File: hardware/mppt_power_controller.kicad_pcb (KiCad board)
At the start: 2 copper layers, 100 x 50 mm, 55 parts, among them J1 Solar Input, J2 USB_B_Micro, J3 Conn_ARM_JTAG_SWD_10, J4 Battery, J5 Curiosity Board, Q1 Q_NMOS_GSD, Q2 Q_NMOS_GSD, U1 INA233, U2 PX3519, U3 ATSAMD21G18A-AUT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

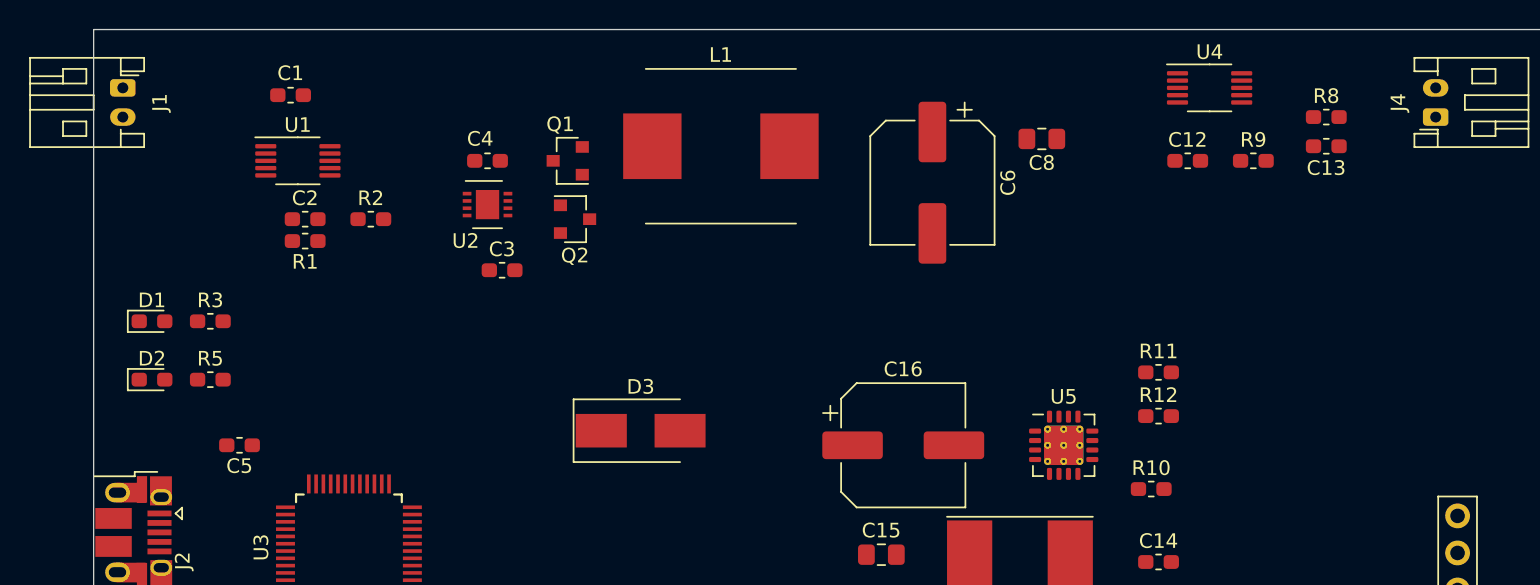
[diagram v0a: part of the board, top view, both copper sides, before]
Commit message: Routed a good portion of the buck converter and the first voltage/current monitor.
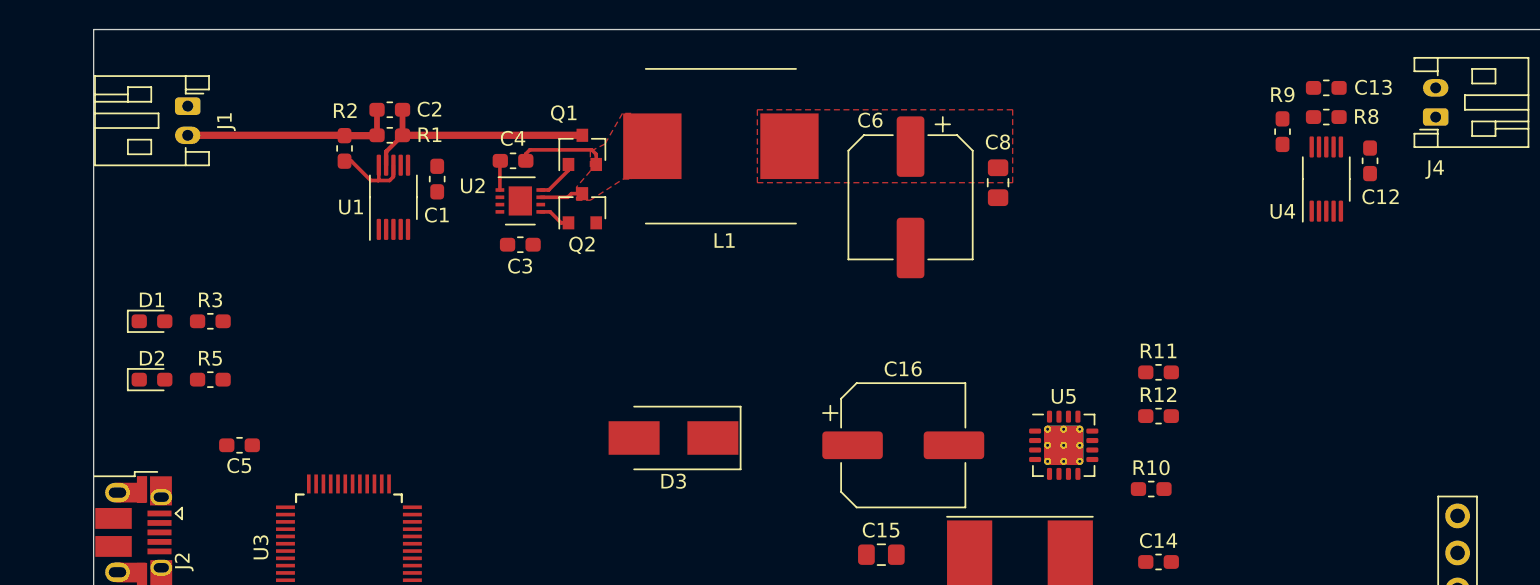
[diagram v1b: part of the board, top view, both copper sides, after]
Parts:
- moved C12 12.5 mm to (157.0, 70.5), turned to -90 degrees
- moved C1 11.6 mm to (93.0, 71.8), turned to -90 degrees
- moved U4 10.2 mm to (154.0, 71.8), turned to 90 degrees
- moved C2 9.48 mm to (89.8, 67.0), turned to 180 degrees
- moved R1 9.28 mm to (89.8, 68.8)
- moved U1 7.01 mm to (90.0, 73.0), turned to 90 degrees
- moved R2 5.17 mm to (86.7, 69.7), turned to 90 degrees
- moved J1 4.62 mm to (76.0, 66.8)
- moved C8 4.24 mm to (131.5, 72.0), turned to -90 degrees
- moved C13 4.00 mm to (154.0, 65.5), turned to 180 degrees
- moved R9 2.83 mm to (151.0, 68.5), turned to 90 degrees
- moved D3 2.30 mm to (109.2, 89.5), turned to 180 degrees
- moved U2 2.26 mm to (98.8, 73.2)
- moved C3 2.15 mm to (98.8, 76.2)
- moved C6 1.80 mm to (125.5, 73.0)
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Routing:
- net Net-(C2-Pad1): track 0.00 -> 16.6 mm
- net Net-(C2-Pad2): track 0.00 -> 14.7 mm
- net Net-(C4-Pad1): track 0.00 -> 9.19 mm
- net Net-(R2-Pad1): track 0.00 -> 5.87 mm
- net Net-(Q1-Pad1): track 0.00 -> 2.86 mm
- net Net-(Q2-Pad1): track 0.00 -> 2.21 mm
- net Net-(C4-Pad2): track 0.00 -> 2.01 mm
- added copper zone on F.Cu, net Net-(C3-Pad1)
- added copper zone on F.Cu, net Net-(C4-Pad1)

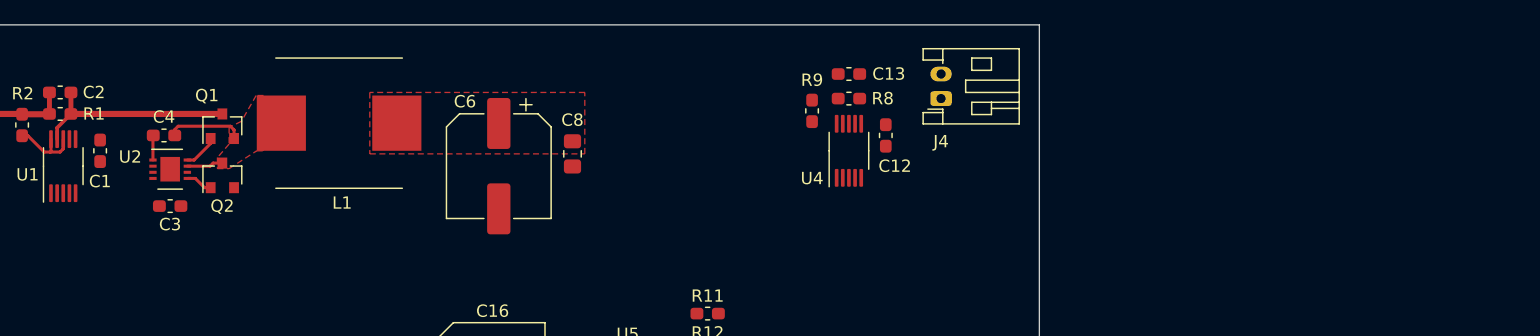
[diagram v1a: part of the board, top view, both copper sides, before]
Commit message: Add four M3 mounting holes so I dont hate myself later.
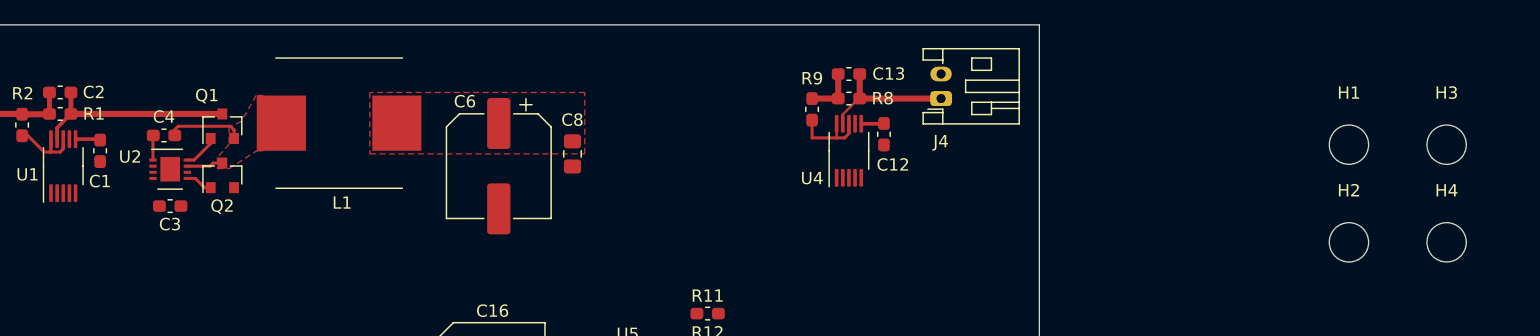
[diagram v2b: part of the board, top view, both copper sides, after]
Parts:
- added H1: MountingHole, MountingHole:MountingHole_3.2mm_M3, F.Cu at (194.7, 71.2)
- added H2: MountingHole, MountingHole:MountingHole_3.2mm_M3, F.Cu at (194.7, 79.2)
- added H3: MountingHole, MountingHole:MountingHole_3.2mm_M3, F.Cu at (202.7, 71.2)
- added H4: MountingHole, MountingHole:MountingHole_3.2mm_M3, F.Cu at (202.7, 79.2)
- moved C12 0.18 mm to (156.8, 70.4)
- moved R9 0.12 mm to (151.0, 68.4)
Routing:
- net /VBat: track 0.00 -> 11.3 mm
- net Net-(R9-Pad1): track 0.00 -> 6.54 mm
- net Net-(C13-Pad2): track 0.00 -> 4.12 mm
- net /3.3V: track 0.00 -> 3.89 mm

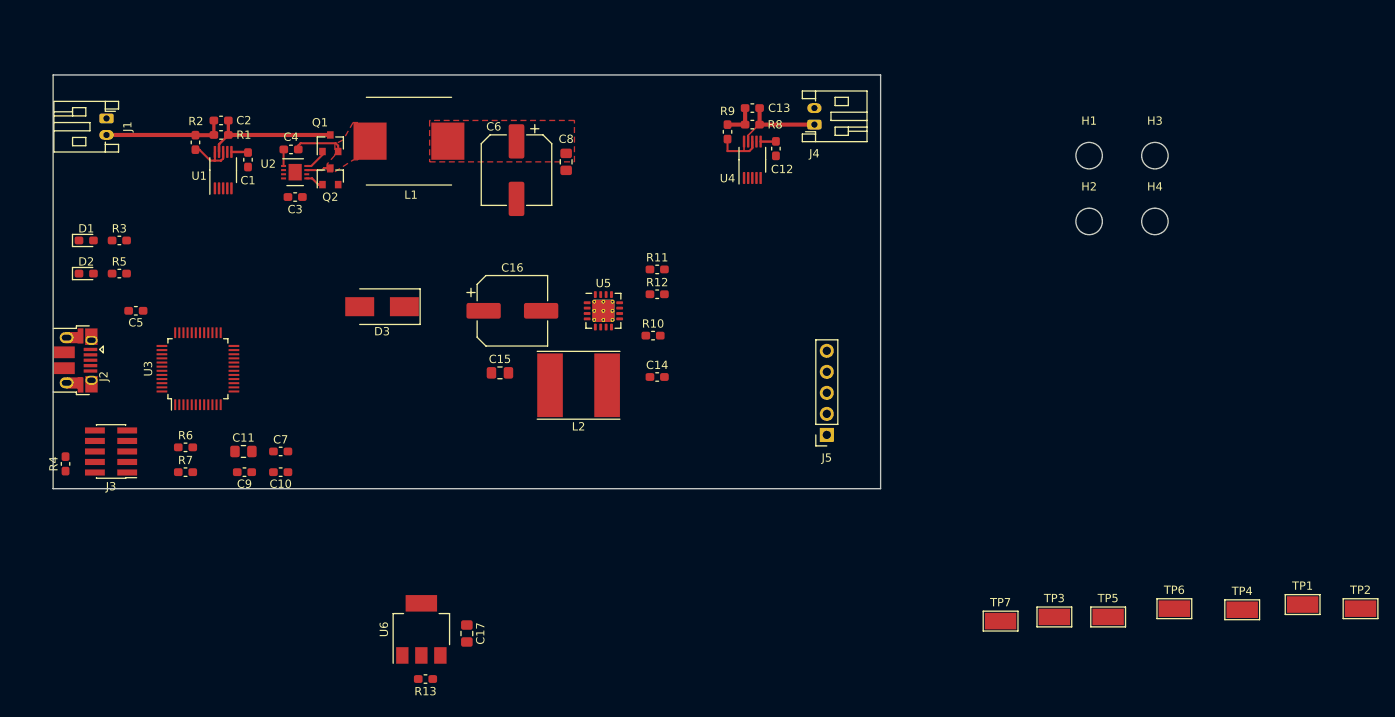
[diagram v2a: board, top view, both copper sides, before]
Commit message: Put mounting holes 5mm in from board edge.
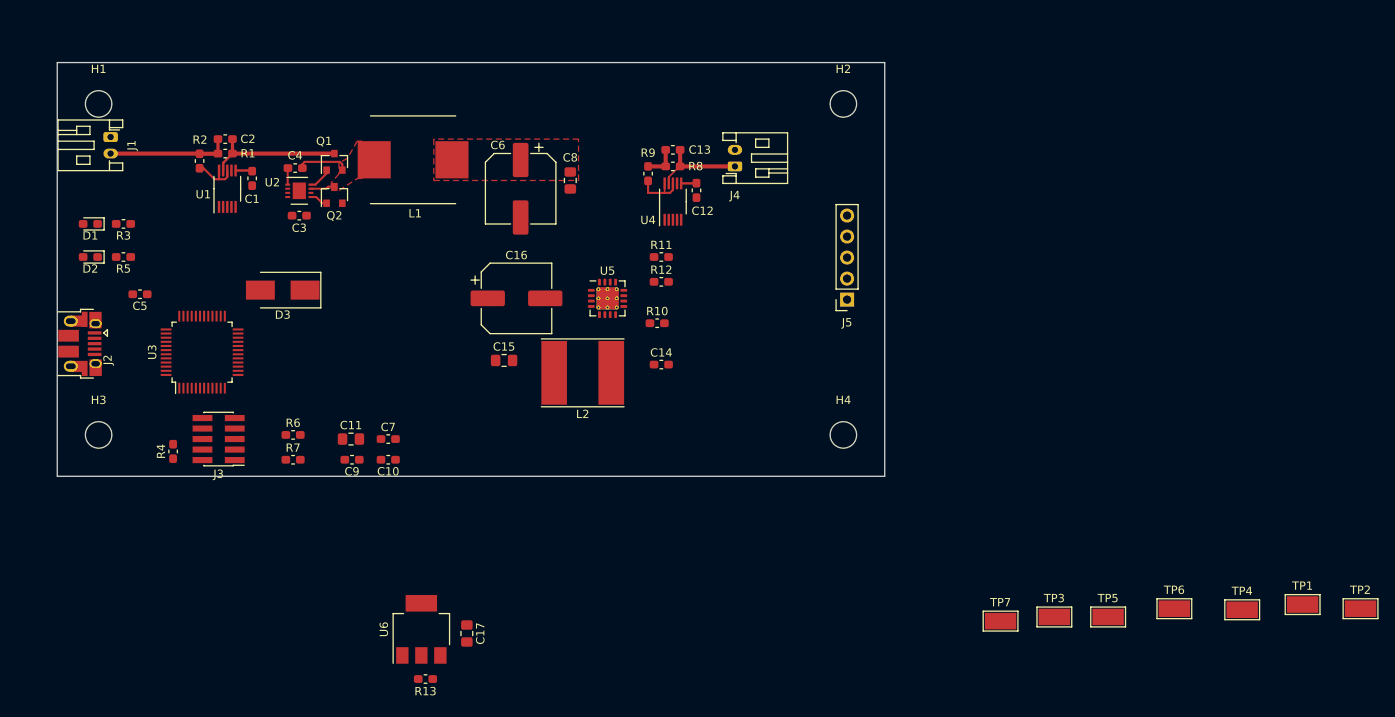
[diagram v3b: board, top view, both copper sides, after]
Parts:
- moved H3 132.0 mm to (75.0, 105.0)
- moved H1 119.9 mm to (75.0, 65.0)
- moved H4 45.6 mm to (165.0, 105.0)
- moved H2 32.9 mm to (165.0, 65.0)
- moved J5 16.5 mm to (165.4, 88.7)
- moved C10 13.1 mm to (110.0, 108.0)
- moved C11 13.1 mm to (105.5, 105.5)
- moved C7 13.1 mm to (110.0, 105.5)
- moved C9 13.1 mm to (105.6, 108.0)
- moved J3 13.1 mm to (89.5, 105.5)
- moved R4 13.1 mm to (84.0, 107.0)
- moved R6 13.1 mm to (98.5, 105.0)
- moved R7 13.1 mm to (98.5, 108.0)
- moved D3 12.2 mm to (97.2, 87.5)
- moved C12 10.8 mm to (147.2, 75.5)
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
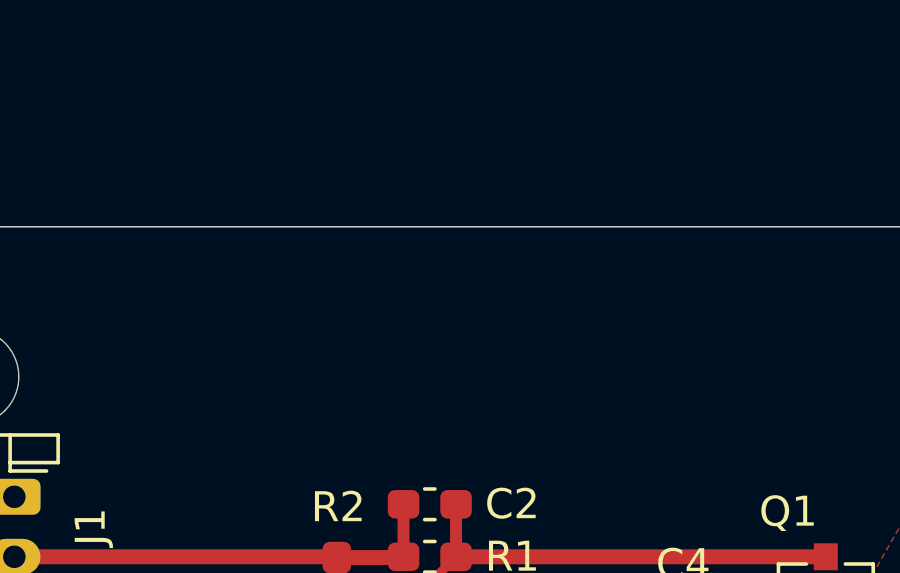
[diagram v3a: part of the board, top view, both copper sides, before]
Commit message: Add some input capacitance for the solar panel
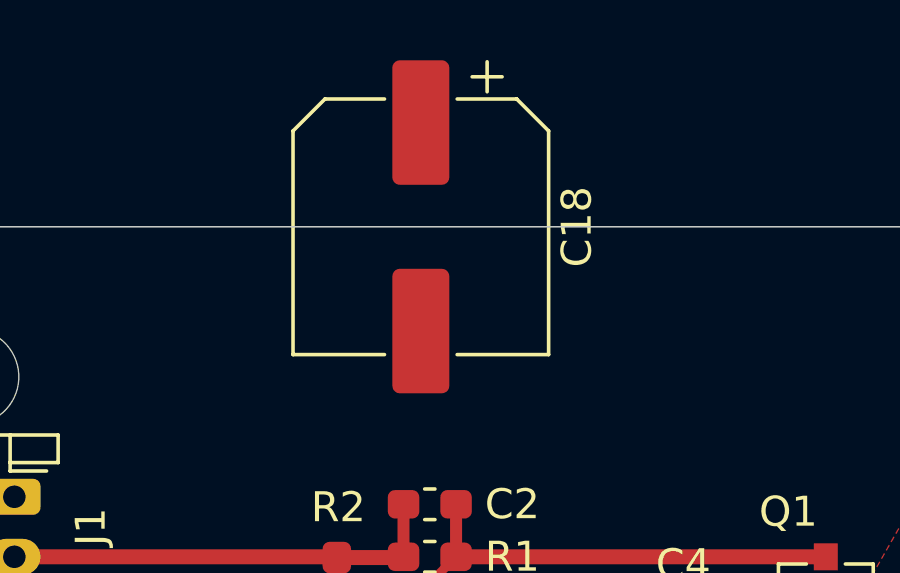
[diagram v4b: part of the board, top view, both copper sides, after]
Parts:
- added C18: 270uF,16V, Capacitor_SMD:CP_Elec_8x6.9, F.Cu at (90.0, 60.0)

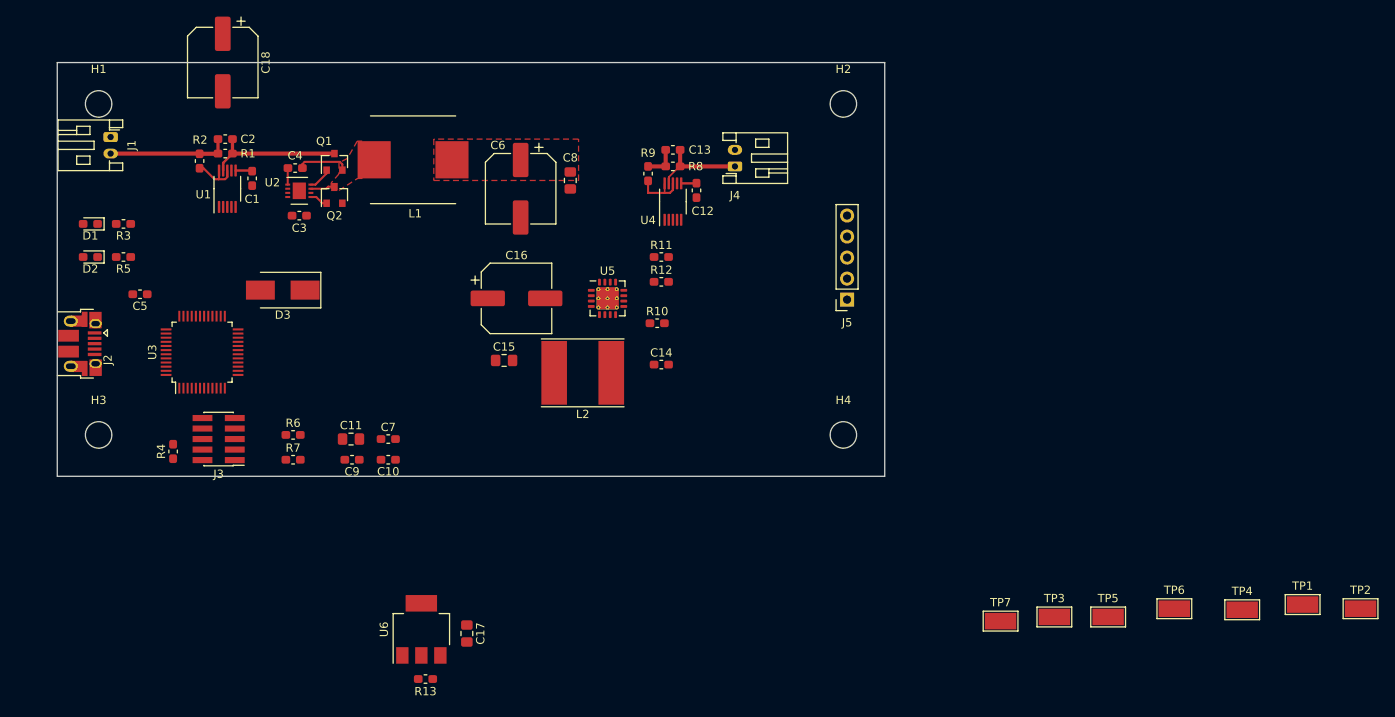
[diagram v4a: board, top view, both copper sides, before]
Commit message: Route a good amount of the microcontroller as well as the 5V power supply.
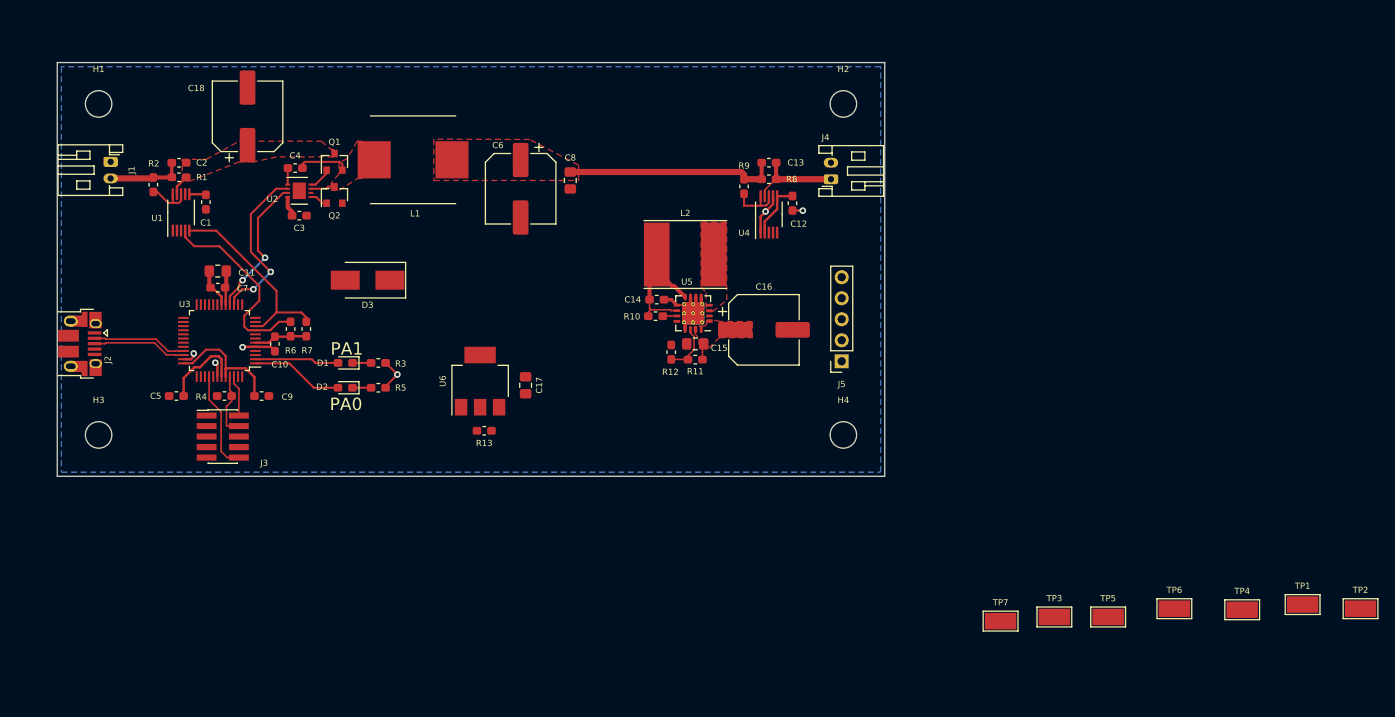
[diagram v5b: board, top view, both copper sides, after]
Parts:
- moved D1 35.1 mm to (104.8, 96.3)
- moved R3 35.1 mm to (108.8, 96.3)
- moved D2 34.6 mm to (104.8, 99.3)
- moved R5 34.6 mm to (108.8, 99.3)
- moved C17 30.8 mm to (126.6, 99.0)
- moved R13 30.8 mm to (121.6, 104.5)
- moved U6 30.8 mm to (121.1, 98.5)
- moved C16 30.1 mm to (155.4, 92.3)
- moved C7 27.6 mm to (89.4, 87.2)
- moved C11 25.9 mm to (89.4, 85.2), turned to 180 degrees
- moved C15 23.2 mm to (147.1, 94.0), turned to 180 degrees
- moved C10 19.6 mm to (96.3, 94.0), turned to 90 degrees
- moved L2 18.9 mm to (145.9, 83.2), turned to 0 degrees
- moved R7 15.9 mm to (100.1, 92.2), turned to 90 degrees
- moved C9 13.4 mm to (94.7, 100.3)
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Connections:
- C2 pad 1: Net-(C2-Pad1) -> Net-(C18-Pad1)
- C2 pad 2: Net-(C18-Pad1) -> Net-(C2-Pad2)
- J1 pad 2: Net-(C18-Pad1) -> Net-(C2-Pad2)
- Q1 pad 3: Net-(C2-Pad1) -> Net-(C18-Pad1)
- R1 pad 1: Net-(C2-Pad1) -> Net-(C18-Pad1)
- R1 pad 2: Net-(C18-Pad1) -> Net-(C2-Pad2)
- R2 pad 2: Net-(C18-Pad1) -> Net-(C2-Pad2)
- TP1 pad 1: Net-(C18-Pad1) -> Net-(C2-Pad2)
- U1 pad 9: Net-(C2-Pad1) -> Net-(C18-Pad1)
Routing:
- net GND: track 0.00 -> 33.2 mm, vias 0 -> 6
- net /3.3V: track 3.89 -> 34.3 mm
- net /SDA: track 0.00 -> 24.0 mm
- net /SCL: track 0.00 -> 23.8 mm
- net Net-(C13-Pad2): track 4.12 -> 25.8 mm
- net /FET_PWM: track 0.00 -> 20.3 mm, vias 0 -> 2
- net /VBat: track 11.3 -> 29.2 mm
- net /FET_ENABLE: track 0.00 -> 17.4 mm, vias 0 -> 2
- net Net-(C2-Pad1): track 16.6 -> 0.00 mm
- net Net-(C18-Pad1): track 14.7 -> 2.52 mm
- net /~RESET: track 0.00 -> 12.1 mm
- net /D-: track 0.00 -> 11.4 mm
- net /D+: track 0.00 -> 11.4 mm
- net Net-(D2-Pad2): track 0.00 -> 11.2 mm
- net Net-(D1-Pad2): track 0.00 -> 10.2 mm
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- added copper zone on F.Cu, net /5V
- added copper zone on B.Cu, net GND
- added copper zone on F.Cu, net Net-(C18-Pad1)
- added copper zone on F.Cu, net Net-(L2-Pad2)
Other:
- board text added: "PA0"
- board text added: "PA1"
